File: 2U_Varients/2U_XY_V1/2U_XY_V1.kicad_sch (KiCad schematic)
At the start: 33 parts, among them CN1 DF11-2DSA-4DP, J2 Conn_01x01, J3 Conn_01x01, J4 Conn_01x01, J5 Conn_01x01, U2 TMP112xxDRL, U3 DRV2605LDGS, U4 TCA4311ADGKR, U5 5040500691, U6 5040500691, U7 VEML6031X00

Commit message: Trying Some Schematic Stuff
Doubling solar cells?
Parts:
- added J6, J7, J8, J9: Conn_01x01, SolarPanelBoards:MountingHoles, symbol Connector_Generic:Conn_01x01
- added SC10, SC11, SC12, SC7, SC8, SC9: SM101K07TF, SolarPanelBoards:KXOB101K08F-TR, symbol Device:Solar_Cell
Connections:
- net GND: now also SC10.2 (-), SC12.2 (-), SC8.2 (-); no longer SC2.2 (-), SC4.2 (-), SC6.2 (-)
- new net: SC4.2 (-), SC9.1 (+)
- new net: SC10.1 (+), SC9.2 (-)
- new net: SC2.2 (-), SC7.1 (+)
- new net: SC11.2 (-), SC12.1 (+)
- new net: SC7.2 (-), SC8.1 (+)
- new net: SC11.1 (+), SC6.2 (-)
- no-connect marks 10 -> 14
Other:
- moved on the sheet: D1, D2, D3, SC1, SC2, SC3, SC4, SC5, SC6

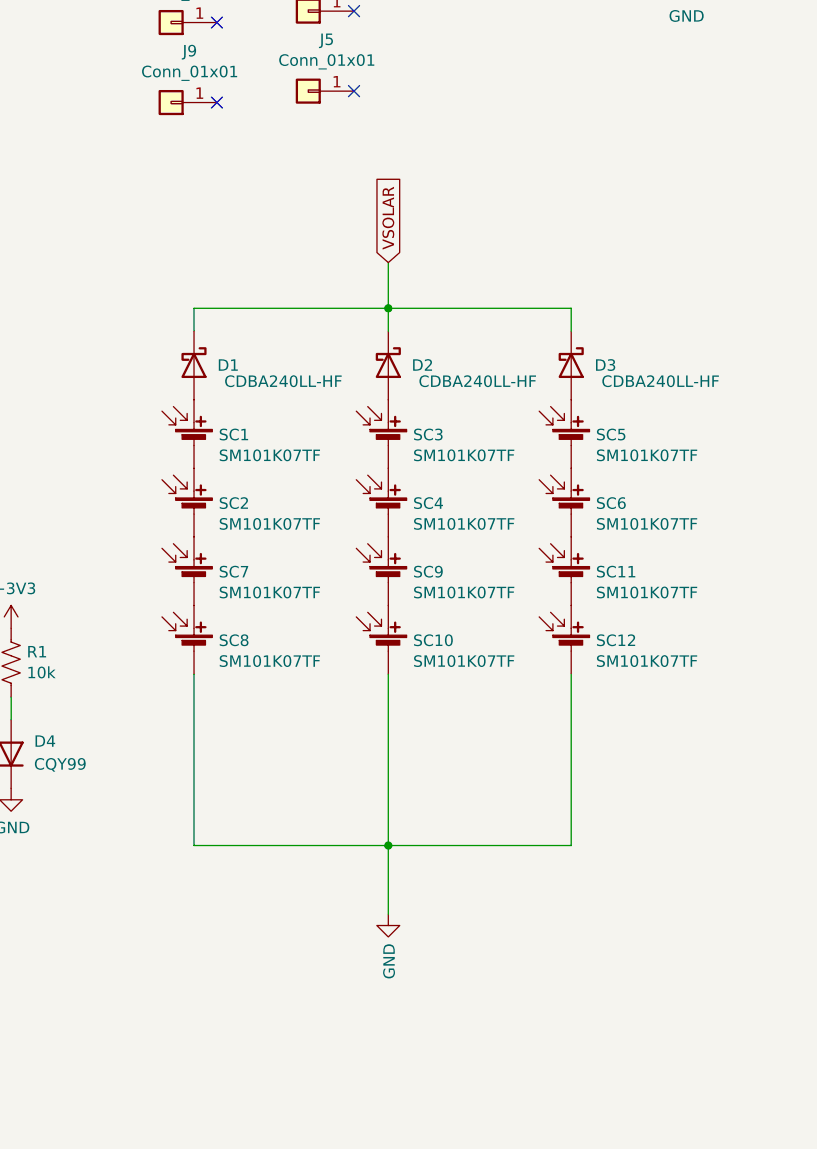
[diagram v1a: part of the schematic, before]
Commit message: Created SM531K10T Libraries
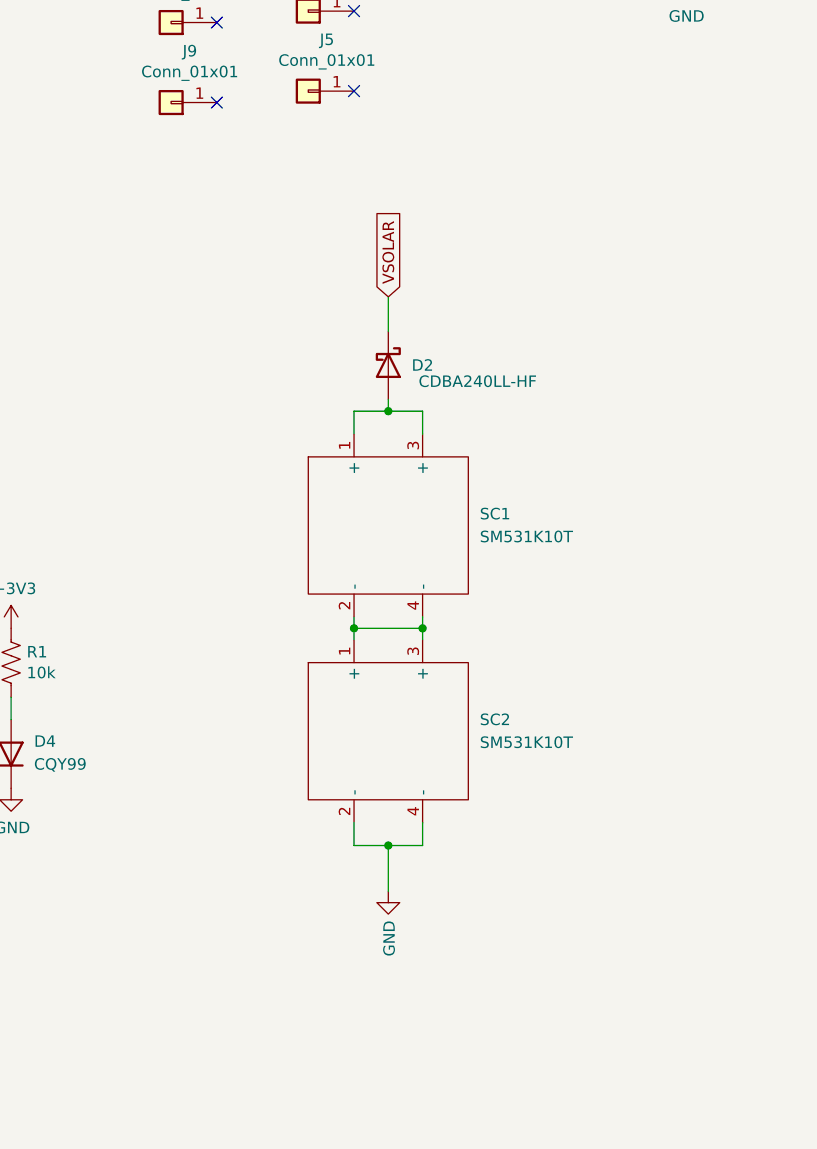
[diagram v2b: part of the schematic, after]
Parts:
- removed D1, D3: CDBA240LL-HF, SolarPanelBoards:DO-214AC, symbol Device:D_Schottky
- removed SC1, SC10, SC11, SC12, SC2, SC3, SC4, SC5, SC6, SC7, SC8, SC9: SM101K07TF, SolarPanelBoards:KXOB101K08F-TR, symbol Device:Solar_Cell
- added SC1, SC2: SM531K10T, Solar_Cell_Library:SM531K10T, symbol solarcell_library:SM531K10T
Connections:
- net GND: now also SC2.2 (-), SC2.4 (-)
- net at D2.2 (A): now also SC1.1 (+), SC1.3 (+)
- new net: SC1.2 (-), SC1.4 (-), SC2.1 (+), SC2.3 (+)

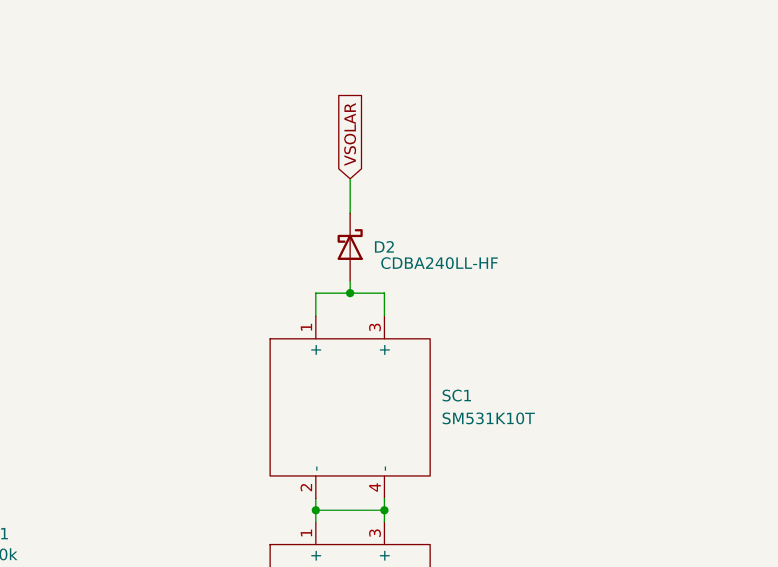
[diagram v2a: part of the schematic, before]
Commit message: Moved Components into the Spot
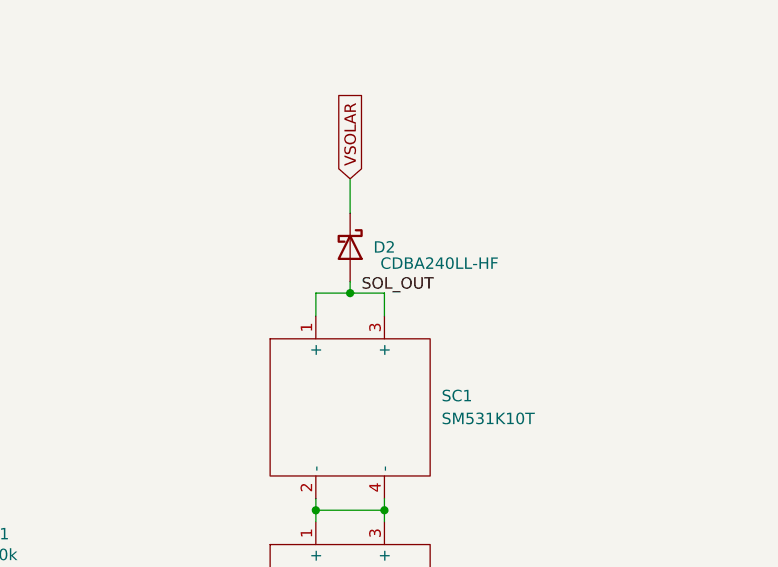
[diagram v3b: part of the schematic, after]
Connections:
- net SOL_OUT: now reaches D2.2 (A), SC1.1 (+), SC1.3 (+)
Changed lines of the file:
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@@
+		)
+	)
+	(label "SOL_OUT"
+		(at 241.3 96.52 0)
+		(effects
+			(font
+				(size 1.27 1.27)
+			)
+			(justify left bottom)
 		)
 	)

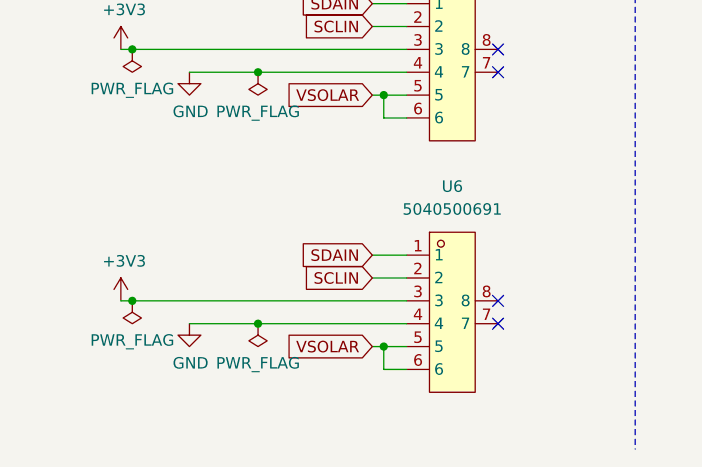
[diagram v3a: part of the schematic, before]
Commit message: Placed the Driver
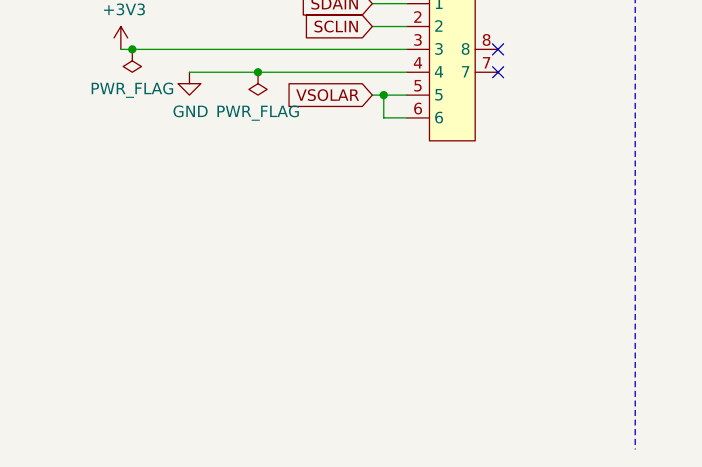
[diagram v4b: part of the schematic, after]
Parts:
- removed U6: 5040500691, easyeda2kicad:CONN-SMD_6P-P1.50_A1501WRB-S-6P, symbol easyeda2kicad:5040500691
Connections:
- no-connect marks 14 -> 12
